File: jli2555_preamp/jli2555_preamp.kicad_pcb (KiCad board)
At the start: 2 copper layers, 24 parts, among them U1 NMA0515SC, U2 TL071, U3 NE5532

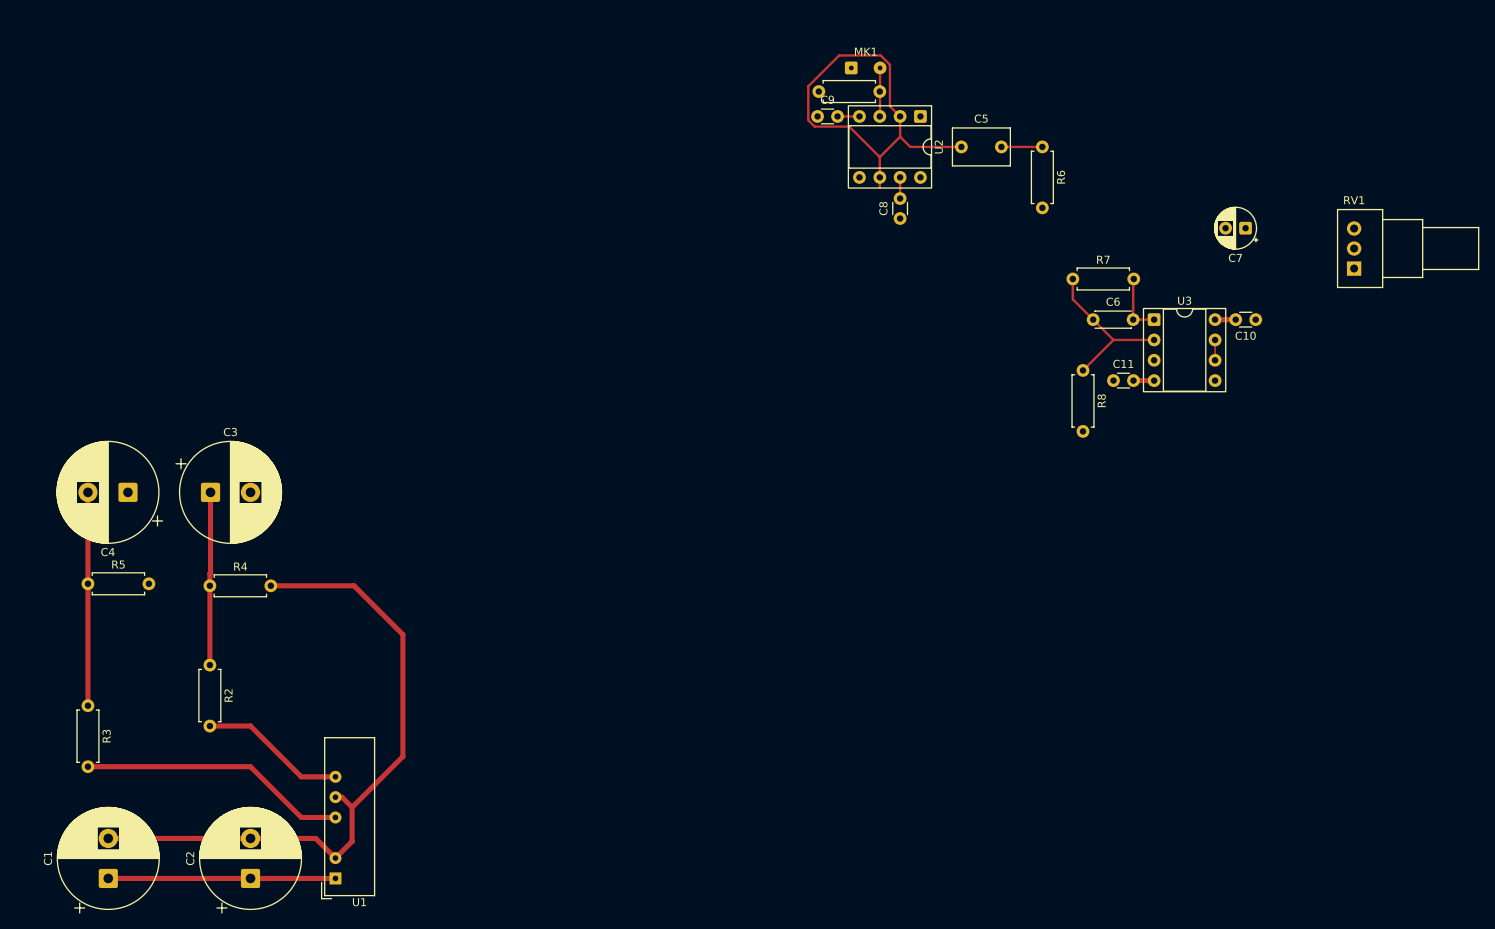
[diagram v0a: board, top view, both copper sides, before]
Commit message: Overhaul of the power supply, will now be a 9v supply for greater simplicity
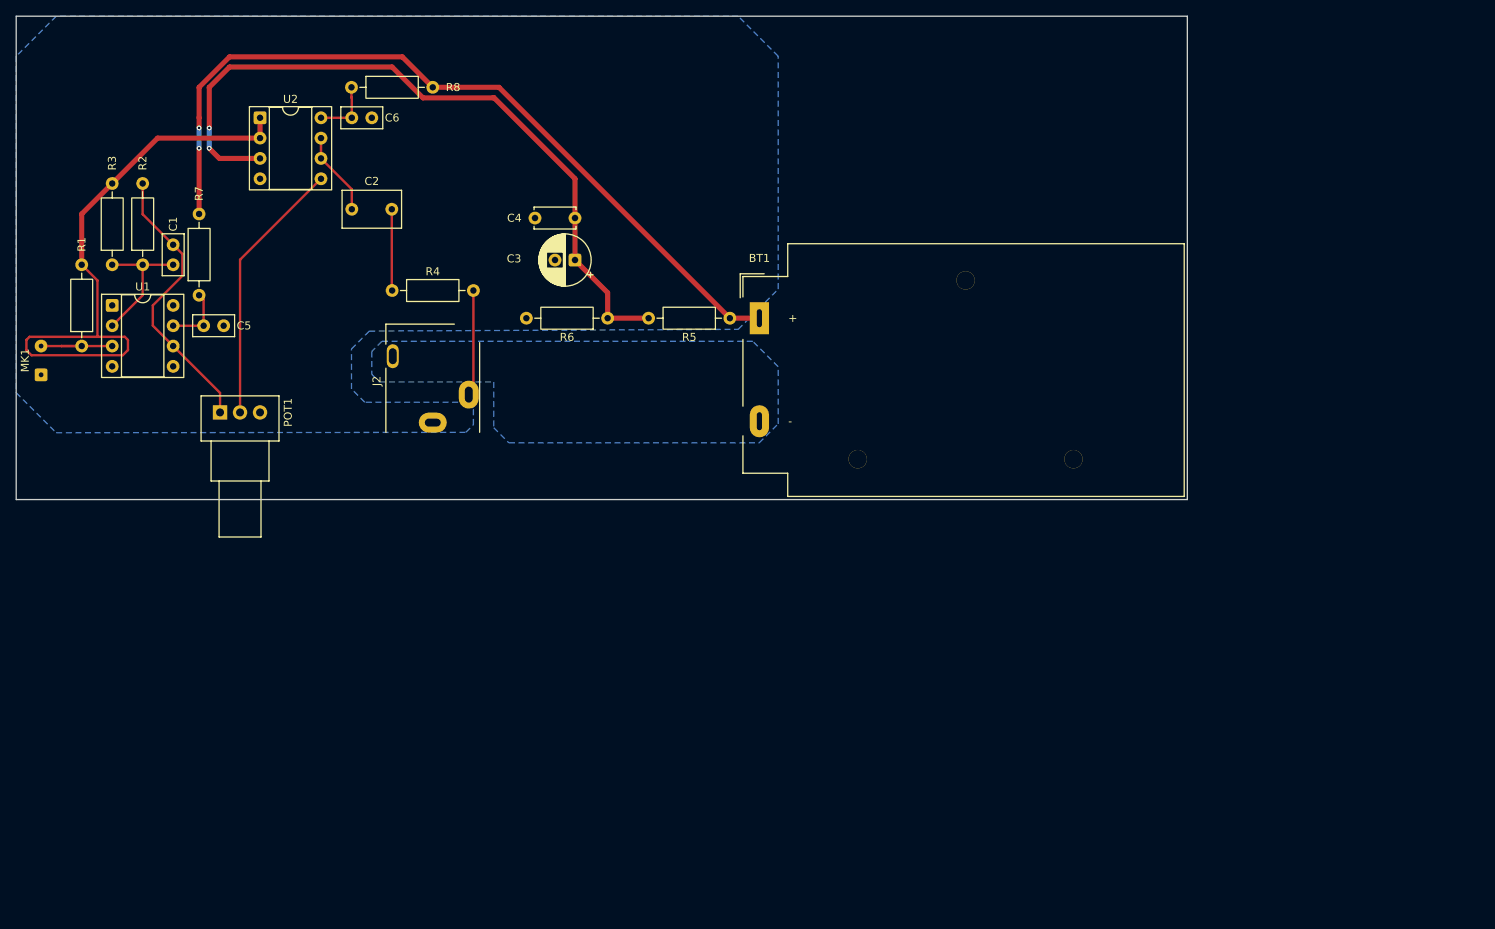
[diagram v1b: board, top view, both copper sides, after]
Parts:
- removed C10, C11, C8, C9: 0u1, Capacitor_THT:C_Disc_D3.0mm_W1.6mm_P2.50mm
- removed C7: 10uF, Capacitor_THT:CP_Radial_D5.0mm_P2.50mm
- removed RV1: R_Potentiometer_US, Potentiometer_THT:Potentiometer_Alps_RK09Y11_Single_Horizontal
- removed U3: NE5532, Package_DIP:DIP-8_W7.62mm_Socket
- added BT1: 9 V, Battery:BatteryHolder_MPD_BA9VPC_1xPP3, F.Cu at (106.9, 53.2)
- added J2: AudioJack3, Connector_Audio:Jack_3.5mm_CUI_SJ1-3513N_Horizontal, F.Cu at (66.0, 66.2)
- added POT1: 100k, Potentiometer_THT:Potentiometer_Alps_RK09Y11_Single_Horizontal, F.Cu at (39.5, 64.9)
- C1: value 2200uF -> 22pF; footprint Capacitor_THT:CP_Radial_D12.5mm_P5.00mm -> Capacitor_THT:C_Disc_D5.0mm_W2.5mm_P2.50mm
- C2: value 2200uF -> 1u; footprint Capacitor_THT:CP_Radial_D12.5mm_P5.00mm -> Capacitor_THT:C_Rect_L7.2mm_W4.5mm_P5.00mm_FKS2_FKP2_MKS2_MKP2
- C3: value 2200u -> 100u; footprint Capacitor_THT:CP_Radial_D12.5mm_P5.00mm -> Capacitor_THT:CP_Radial_D6.3mm_P2.50mm
- C4: value 2200u -> 0u1; footprint Capacitor_THT:CP_Radial_D12.5mm_P5.00mm -> Capacitor_THT:C_Disc_D5.0mm_W2.5mm_P5.00mm
- C5: value 1u -> 0u1; footprint Capacitor_THT:C_Rect_L7.0mm_W4.5mm_P5.00mm -> Capacitor_THT:C_Disc_D5.0mm_W2.5mm_P2.50mm
- C6: value 22pF -> 0u1; footprint Capacitor_THT:C_Disc_D4.3mm_W1.9mm_P5.00mm -> Capacitor_THT:C_Disc_D5.0mm_W2.5mm_P2.50mm
- MK1: value JIL2555 -> JLI2555
- R1: footprint Resistor_THT:R_Axial_DIN0207_L6.3mm_D2.5mm_P7.62mm_Horizontal -> Resistor_THT:R_Axial_DIN0207_L6.3mm_D2.5mm_P10.16mm_Horizontal
- R2: value 100 -> 39k; footprint Resistor_THT:R_Axial_DIN0207_L6.3mm_D2.5mm_P7.62mm_Horizontal -> Resistor_THT:R_Axial_DIN0207_L6.3mm_D2.5mm_P10.16mm_Horizontal
- R3: value 100 -> 1k; footprint Resistor_THT:R_Axial_DIN0207_L6.3mm_D2.5mm_P7.62mm_Horizontal -> Resistor_THT:R_Axial_DIN0207_L6.3mm_D2.5mm_P10.16mm_Horizontal
- R4: value 2k2 -> 100; footprint Resistor_THT:R_Axial_DIN0207_L6.3mm_D2.5mm_P7.62mm_Horizontal -> Resistor_THT:R_Axial_DIN0207_L6.3mm_D2.5mm_P10.16mm_Horizontal
- R5: value 2k2 -> 10k; footprint Resistor_THT:R_Axial_DIN0207_L6.3mm_D2.5mm_P7.62mm_Horizontal -> Resistor_THT:R_Axial_DIN0207_L6.3mm_D2.5mm_P10.16mm_Horizontal
- R6: value 47k -> 10k; footprint Resistor_THT:R_Axial_DIN0207_L6.3mm_D2.5mm_P7.62mm_Horizontal -> Resistor_THT:R_Axial_DIN0207_L6.3mm_D2.5mm_P10.16mm_Horizontal
- R7: value 33k -> 47; footprint Resistor_THT:R_Axial_DIN0207_L6.3mm_D2.5mm_P7.62mm_Horizontal -> Resistor_THT:R_Axial_DIN0207_L6.3mm_D2.5mm_P10.16mm_Horizontal
- R8: value 1k -> 47; footprint Resistor_THT:R_Axial_DIN0207_L6.3mm_D2.5mm_P7.62mm_Horizontal -> Resistor_THT:R_Axial_DIN0207_L6.3mm_D2.5mm_P10.16mm_Horizontal
- U1: value NMA0515SC -> OPA134; footprint Converter_DCDC:Converter_DCDC_Murata_NMAxxxxSC_THT -> Package_DIP:DIP-8_W7.62mm_Socket
- U2: value TL071 -> TL072
- moved R7 109.2 mm to (36.8, 50.3), turned to 90 degrees
- moved MK1 108.3 mm to (17.1, 60.2), turned to 90 degrees
- moved R1 104.7 mm to (22.2, 56.6), turned to 90 degrees
- moved R8 98.0 mm to (55.9, 24.3), turned to 0 degrees
- moved C5 94.9 mm to (39.9, 54.1), turned to 180 degrees
- moved C6 93.6 mm to (58.4, 28.1), turned to 180 degrees
- moved R5 86.8 mm to (103.2, 53.2), turned to 180 degrees
- moved C2 84.6 mm to (55.9, 39.5), turned to 0 degrees
- moved U2 82.6 mm to (44.5, 28.1), turned to 0 degrees
- moved C1 77.1 mm to (33.6, 46.5)
- moved U1 76.9 mm to (26.0, 51.6), turned to 0 degrees
- moved C4 61.4 mm to (78.8, 40.6), turned to 0 degrees
- moved R6 58.4 mm to (87.9, 53.2), turned to 180 degrees
- moved R3 55.2 mm to (26.0, 46.5), turned to 90 degrees
- moved C3 54.0 mm to (83.8, 45.9), turned to 180 degrees
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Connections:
- C1 pad 1: +5V -> Net-(U1A--)
- C1 pad 2: GND -> Net-(C1-Pad2)
- C2 pad 1: +5V -> Net-(U2B--)
- C2 pad 2: GND -> Net-(C2-Pad2)
- C3 pad 1: +15V -> Net-(U2A-+)
- C4 pad 2: -15V -> Net-(U2A-+)
- C5 pad 1: Net-(U2A--) -> GND
- C5 pad 2: Net-(U3A-+) -> Net-(U1B-V+)
- C6 pad 1: Net-(U3A--) -> GND
- C6 pad 2: Net-(C6-Pad2) -> Net-(U2C-V+)
- R1 pad 2: GND -> Vref
- R2 pad 1: +15V -> Net-(U1A--)
- R2 pad 2: Net-(U1-VOUT+) -> Net-(C1-Pad2)
- R3 pad 1: -15V -> Net-(U1A--)
- R3 pad 2: Net-(U1-VOUT-) -> Vref
- R4 pad 1: +15V -> Net-(C2-Pad2)
- R4 pad 2: GND -> Net-(J2-PadT)
- R5 pad 1: -15V -> +9v
- R5 pad 2: GND -> Net-(U2A-+)
- R6 pad 1: Net-(U3A-+) -> Net-(U2A-+)
- R7 pad 1: Net-(U3A--) -> Net-(U1B-V+)
- R7 pad 2: Net-(C6-Pad2) -> +9v
- R8 pad 1: Net-(U3A--) -> Net-(U2C-V+)
- R8 pad 2: GND -> +9v
- U1 pad 1: +5V -> unconnected-(U1B-NC-Pad1)
- U1 pad 2: GND -> Net-(U1A--)
- U1 pad 4: Net-(U1-VOUT-) -> GND
- U1 pad 5: GND -> unconnected-(U1B-NC-Pad5)
- U1 pad 6: Net-(U1-VOUT+) -> Net-(C1-Pad2)
- U2 pad 1: unconnected-(U2B-NULL-Pad1) -> Vref
- U2 pad 2: Net-(U2A--) -> Vref
- U2 pad 3: Net-(MK1-+) -> Net-(U2A-+)
- U2 pad 4: -15V -> GND
- U2 pad 5: unconnected-(U2B-NULL-Pad5) -> Net-(U2B-+)
- U2 pad 6: Net-(U2A--) -> Net-(U2B--)
- U2 pad 7: +15V -> Net-(U2B--)
- U2 pad 8: unconnected-(U2A-NC-Pad8) -> Net-(U2C-V+)
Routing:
- net +9v: track 0.00 -> 101.0 mm, vias 0 -> 2
- net Net-(U2A-+): track 0.00 -> 91.3 mm, vias 0 -> 2
- net GND: track 83.3 -> 0.00 mm
- net Vref: track 0.00 -> 73.7 mm
- net Net-(U2A--): track 52.5 -> 0.00 mm
- net Net-(C1-Pad2): track 0.00 -> 35.8 mm
- net Net-(U1-VOUT-): track 33.6 -> 0.00 mm
- net Net-(U2B-+): track 0.00 -> 33.4 mm
- net -15V: track 32.0 -> 0.00 mm
- net +5V: track 28.6 -> 0.00 mm
- net +15V: track 26.8 -> 0.00 mm
- net Net-(U3A--): track 20.2 -> 0.00 mm
- net Net-(U1-VOUT+): track 18.3 -> 0.00 mm
- net Net-(U1A--): track 0.00 -> 16.8 mm
- net Net-(J2-PadT): track 0.00 -> 13.3 mm
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- added copper zone on B.Cu, net BAT -
- added copper zone on B.Cu, net GND
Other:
- board outline added: 146.4 x 60.4 mm
